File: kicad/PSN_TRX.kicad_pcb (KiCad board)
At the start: 4 copper layers, 220 x 150 mm, 208 parts, among them IC1 LP2950L-5.0V, IC2 NJM2904, J1 RF_IN, J2 SP-OUT, J3 PWR_IN, J4 Volume, J5 Volume, J6 Conn_01x04, J7 I2C_OUT, J8 MIC-IN, K1 G5V-2, Q1 2SC2120, Q10 2SK439, Q11 2SC1815, Q12 2SC1815, Q13 2SC1815, Q14 2SC1815, Q15 2SC1815, Q17 2SC1815, Q2 2SC1815, Q3 3SK59, Q4 2SC1923, Q5 2SC1815, Q6 2SA950, Q7 2SK439, Q8 2SC1971, Q9 2SC1815, T1 ST-71, U1 LP2950-3.3_TO92, U2 Si5351_DIP8, U3 LP2950-3.3_TO92

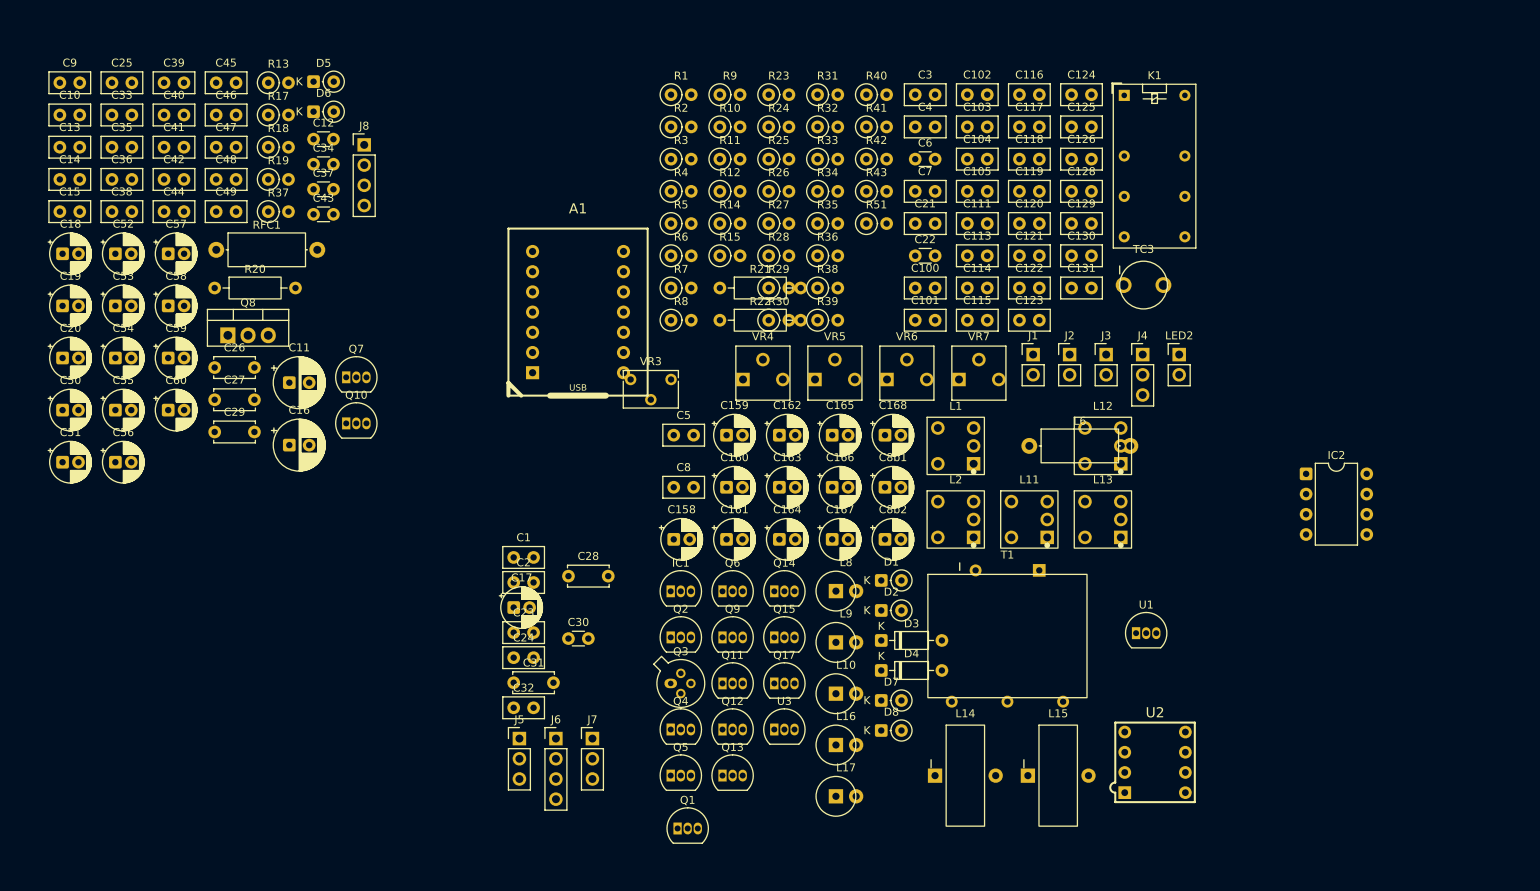
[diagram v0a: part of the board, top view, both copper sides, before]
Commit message: update: KiCadで手動変更した回路図・PCB・プロジェクトファイルを反映
Q3 BF998換装・バイアス回路変更等のKiCad GUI編集内容をコミット。

Co-Authored-By: Claude Sonnet 4.6 <noreply@anthropic.com>
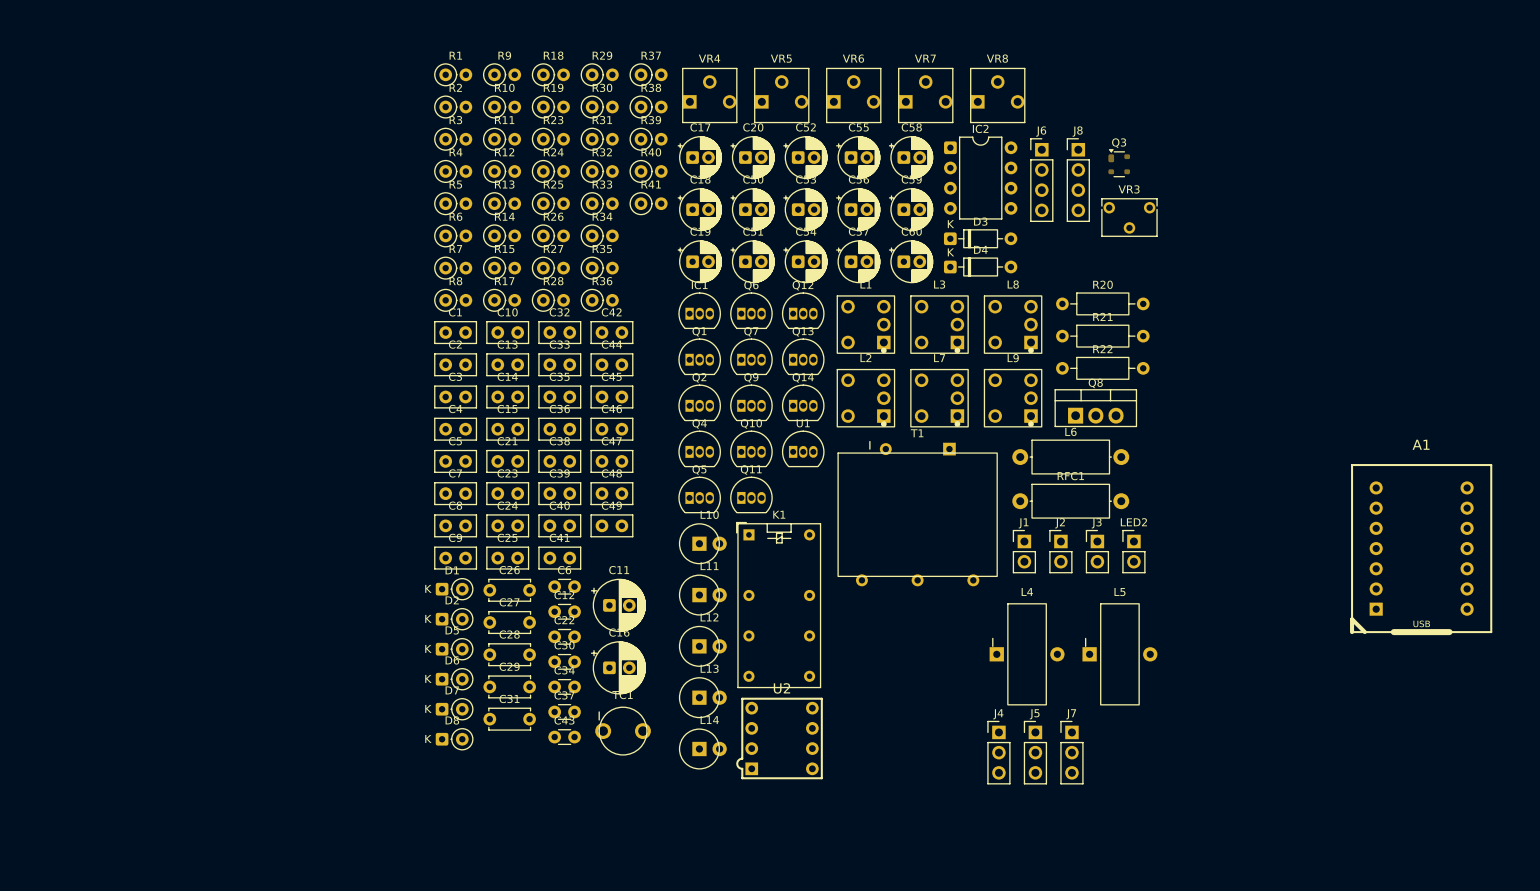
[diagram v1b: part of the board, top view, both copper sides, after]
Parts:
- removed C100, C101, C103, C111, C113, C114, C115, C116, C117, C118, C119, C120, C121, C124, C125, C126: 0.01u, Capacitor_THT:C_Disc_D5.0mm_W2.5mm_P2.50mm
- removed C102, C104, C105, C122, C123: 1u, Capacitor_THT:C_Disc_D5.0mm_W2.5mm_P2.50mm
- removed C128, C129, C130, C131: 47PF, Capacitor_THT:C_Disc_D5.0mm_W2.5mm_P2.50mm
- removed C158, C159, C160, C161, C162, C163, C164, C165, C166, C167, C168: 1u, Capacitor_THT:CP_Radial_D5.0mm_P2.00mm
- removed C8b1, C8b2: 10u, Capacitor_THT:CP_Radial_D5.0mm_P2.00mm
- removed L15: T-50-10 18T/0.4mm, PSN_TRX:L_T50_2pin_Vertical
- removed L16, L17: 100nH, PSN_TRX:L_AL0510-153K_Vertical
- removed Q15, Q17: 2SC1815, Package_TO_SOT_THT:TO-92_Inline
- removed R42: 100k, Resistor_THT:R_Axial_DIN0207_L6.3mm_D2.5mm_P2.54mm_Vertical
- removed R43: 330, Resistor_THT:R_Axial_DIN0207_L6.3mm_D2.5mm_P2.54mm_Vertical
- removed R51: 51, Resistor_THT:R_Axial_DIN0207_L6.3mm_D2.5mm_P2.54mm_Vertical
- removed TC3: 30p, PSN_TRX:C_Trimmer_TMCV01
- removed U3: LP2950-3.3_TO92, Package_TO_SOT_THT:TO-92_Inline
- added L3: 7T50, PSN_TRX:L_FCZ07S_CT, F.Cu at (142.1, 70.9)
- added L4: T-50-10 18T/0.4mm, PSN_TRX:L_T50_2pin_Vertical, F.Cu at (149.3, 112.4)
- added L5: T-50-10 18T/0.4mm, PSN_TRX:L_T50_2pin_Vertical, F.Cu at (161.0, 112.4)
- added L7: 7T50, PSN_TRX:L_FCZ07S_CT, F.Cu at (142.1, 80.2)
- added TC1: 30p, PSN_TRX:C_Trimmer_TMCV01, F.Cu at (99.8, 122.0)
- added VR8: 10k, PSN_TRX:Potentiometer_TOCOS_GF063P_Vertical, F.Cu at (146.9, 42.9)
- L11, L12, L13: footprint PSN_TRX:L_FCZ07S_CT -> PSN_TRX:L_AL0510-153K_Vertical
- L14: footprint PSN_TRX:L_T50_2pin_Vertical -> PSN_TRX:L_AL0510-153K_Vertical
- L8, L9: footprint PSN_TRX:L_AL0510-153K_Vertical -> PSN_TRX:L_FCZ07S_CT
- Q3: value 3SK59 -> BF998; footprint Package_TO_SOT_THT:TO-72-4 -> PSN_TRX:BF998_SOT143
- Q8: value 2SC1971 -> RD06HVF1
- moved A1 110.1 mm to (202.7, 99.1)
- moved Q8 107.0 mm to (159.2, 82.4)
- moved R20 106.6 mm to (157.6, 68.3)
- moved RFC1 105.9 mm to (152.3, 93.1)
- moved C55 97.8 mm to (131.0, 49.9)
- moved C56 97.8 mm to (131.0, 56.5)
- moved J6 96.0 mm to (155.0, 48.9)
- moved C58 94.3 mm to (137.6, 49.9)
- moved C59 94.3 mm to (137.6, 56.5)
- moved C60 94.3 mm to (137.6, 63.0)
- moved J8 89.8 mm to (159.6, 48.9)
- moved C20 89.5 mm to (117.7, 49.9)
- moved C50 89.5 mm to (117.7, 56.5)
- moved C51 89.5 mm to (117.7, 63.0)
- moved C52 86.7 mm to (124.3, 49.9)
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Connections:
- A1 pad 1: (no net) -> Net-(A1-D0/A0)
- A1 pad 10: (no net) -> unconnected-(A1-3V3-Pad10)
- A1 pad 11: (no net) -> unconnected-(A1-D10/MOSI-Pad11)
- A1 pad 12: (no net) -> unconnected-(A1-D9/MISO-Pad12)
- A1 pad 13: (no net) -> unconnected-(A1-D8/SCK-Pad13)
- A1 pad 14: (no net) -> unconnected-(A1-D7/RX-Pad14)
- A1 pad 2: (no net) -> Net-(A1-D1/A1)
- A1 pad 3: (no net) -> Net-(A1-D2/A2)
- A1 pad 4: (no net) -> unconnected-(A1-D3/A3-Pad4)
- A1 pad 5: (no net) -> Net-(A1-D4/SDA)
- A1 pad 6: (no net) -> Net-(A1-D5/SCL)
- A1 pad 7: (no net) -> unconnected-(A1-D6/TX-Pad7)
- A1 pad 8: (no net) -> +5V
- A1 pad 9: (no net) -> GND
- Q3 pad 1: Net-(L1-AA) -> Net-(L2-SA)
- Q3 pad 3: Net-(L2-SA) -> Net-(J5-Pin_2)
- Q3 pad 4: Net-(J5-Pin_2) -> Net-(L1-AA)
- Q8 pad 3: Net-(Q8-E) -> GND
- U2 pad 1: (no net) -> unconnected-(U2-VDDO-Pad1)
- U2 pad 2: (no net) -> Net-(A1-D5/SCL)
- U2 pad 3: (no net) -> Net-(A1-D4/SDA)
- U2 pad 4: (no net) -> GND
- U2 pad 5: (no net) -> Net-(U2-CLK0)
- U2 pad 6: (no net) -> Net-(U2-CLK1)
- U2 pad 7: (no net) -> unconnected-(U2-CLK2-Pad7)
- U2 pad 8: (no net) -> Net-(U1-VO)
- VR3 pad 3: Net-(D3-K) -> GND

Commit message: Rename project from PSN_TRX_Nano_R4 to PSN_TRX_XIAO_SAMD21
- Update README.md title
- Update KiCad project files

Co-Authored-By: Claude Haiku 4.5 <noreply@anthropic.com>
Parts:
- removed D3, D4: 1N4148, Diode_THT:D_DO-35_SOD27_P7.62mm_Horizontal
- removed H1, H2, H3, H4: MountingHole_3.2mm_M3, MountingHole_3.2mm_M3
- removed R20: 10, Resistor_THT:R_Axial_DIN0207_L6.3mm_D2.5mm_P10.16mm_Horizontal
- removed VR1, VR2: 10k, PSN_TRX:Potentiometer_TOCOS_GF063P_Vertical
- J5: moved to B.Cu
- moved J3 138.1 mm to (32.0, 51.5)
- moved J1 136.8 mm to (31.5, 35.0)
- moved J5 115.5 mm to (62.5, 52.0), turned to 90 degrees
- moved Q1 107.4 mm to (57.4, 168.6)
- moved K1 99.1 mm to (41.5, 34.5)
- moved C9 98.7 mm to (161.5, 44.5)
- moved IC1 94.7 mm to (60.9, 150.1)
- moved Q3 87.8 mm to (78.0, 37.0)
- moved L2 84.7 mm to (60.0, 37.0)
- moved R7 80.7 mm to (156.5, 38.0)
- moved Q6 79.9 mm to (102.4, 148.1)
- moved U1 79.6 mm to (102.4, 163.6)
- moved C11 76.4 mm to (93.5, 182.3)
- moved C18 76.4 mm to (104.0, 132.6)
- moved C24 76.4 mm to (79.5, 172.3)
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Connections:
- C6 pad 1: Net-(L1-AA) -> Net-(L1-SA)
- C7 pad 1: Net-(L1-SA) -> Net-(L1-AA)
- L1 pad 3: GND -> +9V
- L1 pad 5: +9V -> GND
- Q3 pad 4: Net-(L1-AA) -> Net-(L1-SA)

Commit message: update: KiCadで手動変更したPCBフットプリント配置を反映
C9・R8・J4のフットプリント位置・回転をPCBエディタで調整した内容をコミット。

Co-Authored-By: Claude Sonnet 4.6 <noreply@anthropic.com>
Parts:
- moved Q1 180.4 mm to (183.0, 39.0)
- moved C11 179.1 mm to (197.5, 36.5)
- moved C5 153.3 mm to (160.0, 38.0)
- moved C16 151.7 mm to (180.0, 65.5)
- moved R14 146.8 mm to (201.0, 54.0)
- moved J4 144.5 mm to (150.0, 54.0), turned to -90 degrees
- moved J2 141.0 mm to (215.0, 49.0)
- moved R6 137.1 mm to (169.0, 38.0)
- moved J7 134.8 mm to (219.0, 81.5)
- moved R8 134.1 mm to (171.5, 53.0)
- moved Q6 128.9 mm to (185.5, 49.5), turned to 180 degrees
- moved U2 125.1 mm to (181.8, 89.3), turned to 180 degrees
- moved C10 124.8 mm to (161.0, 53.5)
- moved C1 112.4 mm to (134.5, 54.0)
- moved R5 105.6 mm to (155.5, 66.0)
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
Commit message: Update component footprints and settings
- LED2: set on_board to 'no'
- R21, R22: change footprint from P10.16mm_Horizontal to P5.08mm_Vertical

Co-Authored-By: Claude Haiku 4.5 <noreply@anthropic.com>
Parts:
- removed C26: 1000pF, Capacitor_THT:C_Disc_D5.0mm_W2.5mm_P5.00mm
- removed LED2: LED黄, Connector_PinHeader_2.54mm:PinHeader_1x02_P2.54mm_Vertical
- added J9: TX-ON-LED, Connector_PinHeader_2.54mm:PinHeader_1x02_P2.54mm_Vertical, F.Cu at (23.0, 83.7)
- J5: moved to F.Cu
- R21, R22: footprint Resistor_THT:R_Axial_DIN0207_L6.3mm_D2.5mm_P10.16mm_Horizontal -> Resistor_THT:R_Axial_DIN0207_L6.3mm_D2.5mm_P5.08mm_Vertical
- moved L4 154.1 mm to (29.3, 83.5)
- moved L5 147.2 mm to (50.7, 83.5)
- moved RFC1 138.5 mm to (26.6, 97.5)
- moved Q8 126.5 mm to (35.5, 109.5), turned to 90 degrees
- moved TC1 124.5 mm to (41.8, 84.5)
- moved C60 122.1 mm to (14.1, 175.8)
- moved J6 122.1 mm to (31.4, 161.8)
- moved C17 122.1 mm to (-12.5, 162.7)
- moved C18 122.1 mm to (-12.5, 169.3)
- moved C19 122.1 mm to (-12.5, 175.8)
- moved C20 122.1 mm to (-5.84, 162.7)
- moved C21 122.1 mm to (-37.0, 200.9)
- moved C22 122.1 mm to (-29.8, 223.0)
- moved C23 122.1 mm to (-37.0, 205.0)
- moved C24 122.1 mm to (-37.0, 209.0)
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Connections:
- Q11 pad 2: Net-(LED2-K) -> Net-(J9-Pin_1)
- R25 pad 1: Net-(LED2-K) -> Net-(J9-Pin_2)
